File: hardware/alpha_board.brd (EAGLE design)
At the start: 22 parts, among them Y1 32.768kHz

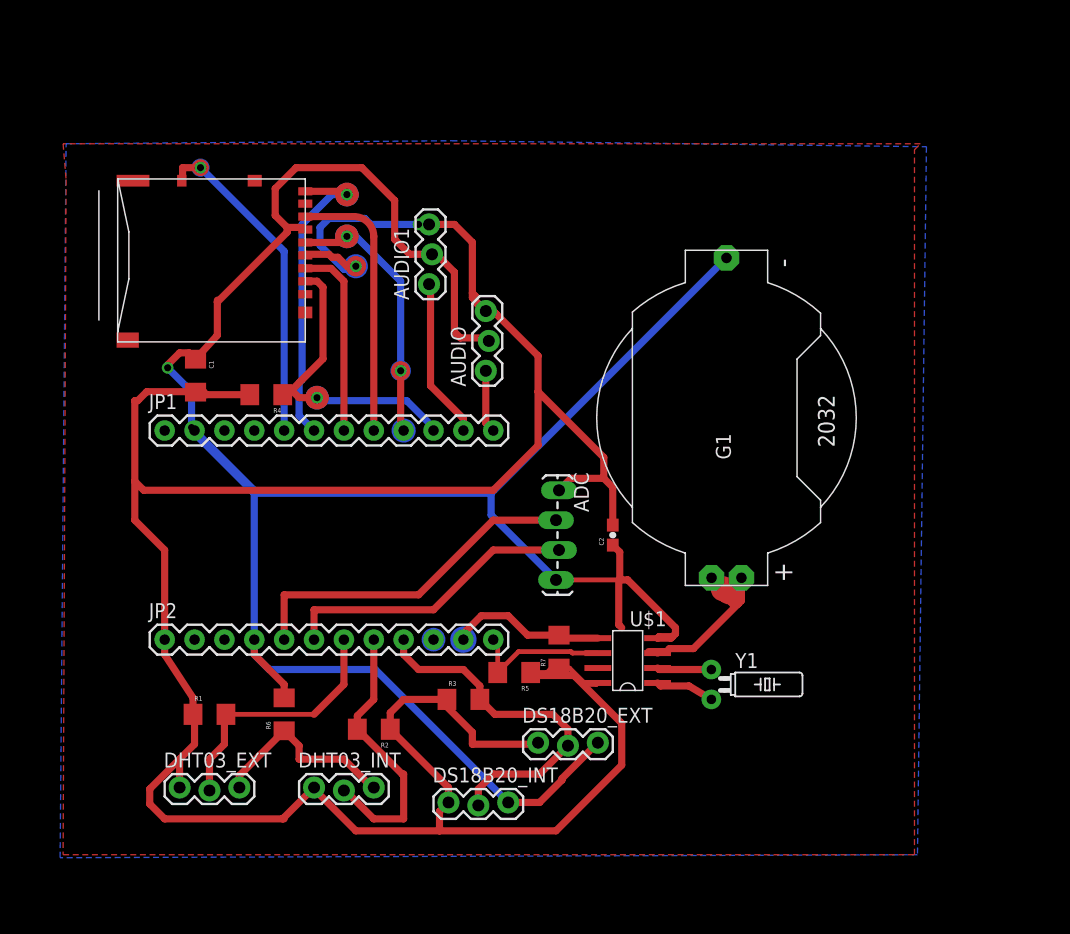
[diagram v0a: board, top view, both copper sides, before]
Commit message: hardware update, new RTC chip, smaller footprint
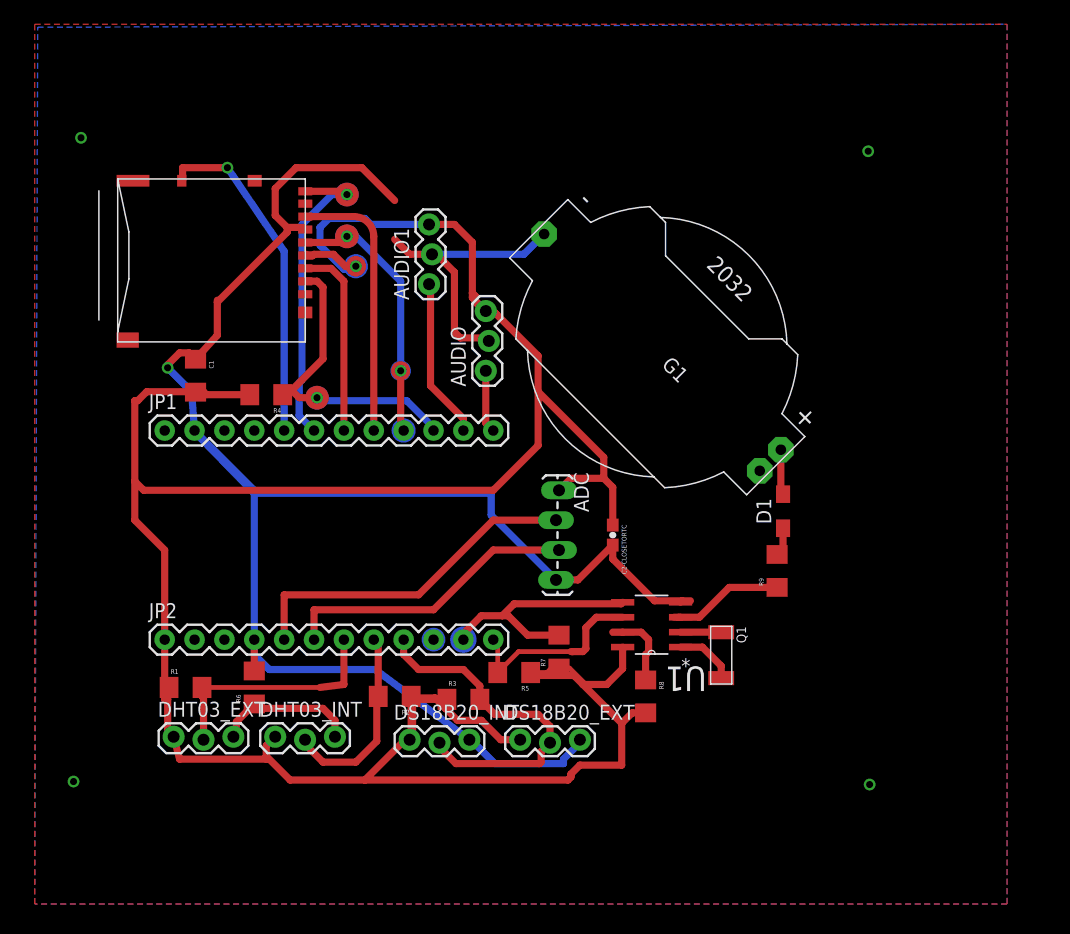
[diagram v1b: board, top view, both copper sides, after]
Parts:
- removed U$1: DS1340, carrilib:SO08
- removed Y1: 32.768kHz, SparkFun-FreqCtrl:TC26H
- added D1: (no value), diode:SOD323-W
- added Q1: (no value), Hangar:ABS10
- added R8: 4.7k, SparkFun:1206
- added R9: 1k, SparkFun:1206
- added U1: MCP79400-I/SN, Microchip-MCP79400-I_SN:SOIC127P600X175-8N
- moved G1 8.42 mm to (48.2, 46.5), turned to 135 degrees
- moved DS18B20_INT 6.27 mm to (27.2, 13.0)
- moved DHT03_INT 5.44 mm to (15.7, 13.2)
- moved DHT03_EXT 4.35 mm to (7.11, 13.2)
- moved R6 3.42 mm to (14.0, 17.5)
- moved R2 3.31 mm to (25.9, 16.8)
- moved R1 3.06 mm to (8.13, 17.5)
- moved DS18B20_EXT 1.55 mm to (36.6, 13.0)
- turned C2-CLOSETORTC to 270 degrees
- renumbered C2 to C2-CLOSETORTC
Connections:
- new net N$10: D1.A, G1.+
- new net N$12: R9.1, U1.3
- new net N$8: R8.1, U1.7
- net GND: now also C2-CLOSETORTC.2, U1.4; no longer C2-CLOSETORTC.1, U$1.4
- net N$11: now also U1.5; no longer U$1.5
- net N$3: now also Q1.1, U1.2; no longer U$1.1, Y1.2
- net N$4: now also Q1.2, U1.1; no longer G1.+, U$1.3
- net N$5: now also D1.C, R9.2; no longer U$1.2, Y1.1
- net N$9: now also U1.6; no longer U$1.6
- net VCC: now also C2-CLOSETORTC.1, R8.2, U1.8; no longer C2-CLOSETORTC.2, U$1.8
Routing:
- net GND: track 212.2 -> 176.8 mm, vias 2 -> 3
- net N$12: track 0.00 -> 9.81 mm
- net N$11: track 13.4 -> 21.0 mm
- net D4: track 23.8 -> 16.9 mm
- net N$8: track 0.00 -> 6.84 mm
- net N$4: track 11.8 -> 5.15 mm
- net VCC: track 245.6 -> 241.0 mm
- net N$9: track 12.3 -> 16.7 mm
- net N$10: track 0.00 -> 3.85 mm
- net GNDR: track 16.7 -> 13.1 mm
- net N$5: track 4.62 -> 2.44 mm
- net N$3: track 4.99 -> 3.46 mm
- net D5: track 21.9 -> 20.5 mm
- net A6: track 28.0 -> 28.8 mm
- net D3: track 30.7 -> 30.1 mm
- added copper zone on layer 1, net N$13
- removed copper zone on layer 1, net GND

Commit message: new PCB design without external RTC, thanks Angel M!
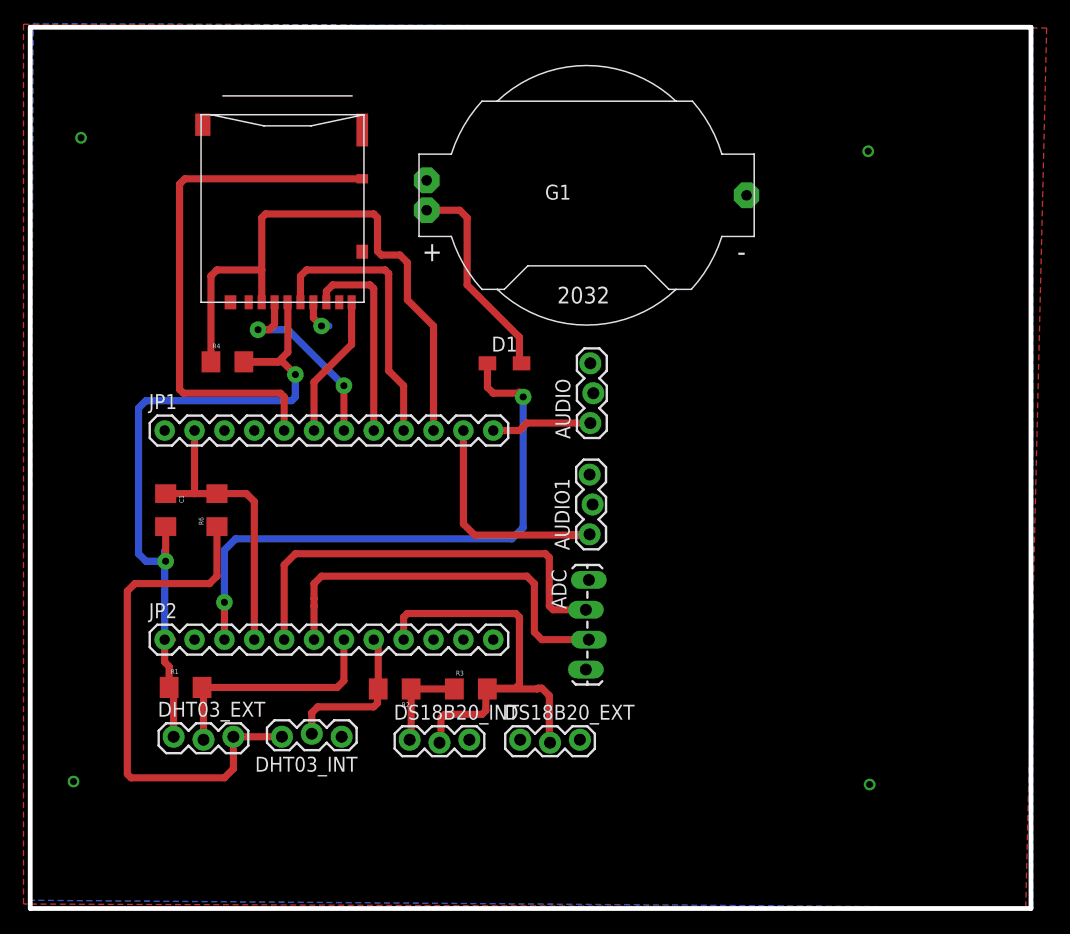
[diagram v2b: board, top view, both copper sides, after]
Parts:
- removed C2-CLOSETORTC: 0.1uF, SparkFun-Capacitors:0603-CAP
- removed Q1: (no value), Hangar:ABS10
- removed R5, R7, R8: 4.7k, SparkFun:1206
- removed R9: 1k, SparkFun:1206
- removed U1: MCP79400-I/SN, Microchip-MCP79400-I_SN:SOIC127P600X175-8N
- moved D1 26.8 mm to (35.2, 45.1), turned to 0 degrees
- moved AUDIO1 25.3 mm to (42.6, 30.5)
- moved R6 15.4 mm to (10.8, 32.6)
- moved G1 14.2 mm to (42.2, 59.4), turned to 0 degrees
- moved C1 11.7 mm to (6.43, 32.6)
- moved AUDIO 9.94 mm to (42.7, 40.0)
- moved ADC 8.03 mm to (42.4, 26.7)
- moved DHT03_INT 5.66 mm to (21.4, 13.5), turned to 180 degrees
- moved R4 4.33 mm to (11.7, 45.2), turned to 0 degrees
- moved U$2 4.26 mm to (16.8, 50.3), turned to 180 degrees
- moved R3 1.09 mm to (32.4, 17.4)
- moved R2 0.64 mm to (25.9, 17.4)
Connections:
- removed net N$11: JP2.11, R7.2, U1.5
- removed net N$12: R9.1, U1.3
- removed net N$3 (its old number): Q1.1, U1.2
- removed net N$5: D1.C, R9.2
- removed net N$8: R8.1, U1.7
- removed net N$9: JP2.12, R5.2, U1.6
- net GND: no longer C2-CLOSETORTC.2, U1.4
- net N$4: now also JP2.11; no longer Q1.2, U1.1
- net VCC: no longer C2-CLOSETORTC.1, R5.1, R7.1, R8.2, U1.8
- net VDDA: now also D1.C
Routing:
- net VCC: track 241.0 -> 72.9 mm
- net GND: track 176.8 -> 27.9 mm, vias 3 -> 1
- net VDDA: track 0.00 -> 50.3 mm, vias 0 -> 2
- net GNDR: track 13.1 -> 44.2 mm
- net N$1: track 26.1 -> 50.1 mm, vias 1 -> 0
- net N$11: track 21.0 -> 0.00 mm
- net N$9: track 16.7 -> 0.00 mm
- net A6: track 28.8 -> 45.2 mm, vias 1 -> 0
- net A7: track 26.7 -> 12.2 mm, vias 1 -> 0
- net N$3: track 3.85 -> 18.0 mm
- net N$12: track 9.81 -> 0.00 mm
- net D3: track 30.1 -> 38.4 mm
- net D6: track 25.5 -> 33.0 mm
- net D7: track 29.6 -> 36.8 mm
- net N$8: track 6.84 -> 0.00 mm
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- added copper zone on layer 1, net VCC
- removed copper zone on layer 1, net N$13
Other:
- board outline added: 85.1 x 74.9 mm
